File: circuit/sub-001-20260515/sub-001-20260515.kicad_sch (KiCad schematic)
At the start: 51 parts, among them SW1 SW_SPDT, SW2 SW_SPDT, SW3 SW_SPDT, U10 LD1117S12TR_SOT223, U11 LD1117S12TR_SOT223, U12 LD1117S12TR_SOT223, U13 TSSP58038, U14 TSSP58038, U15 TSSP58038, U16 TSSP58038, U8 LD1117S12TR_SOT223, U9 LD1117S12TR_SOT223

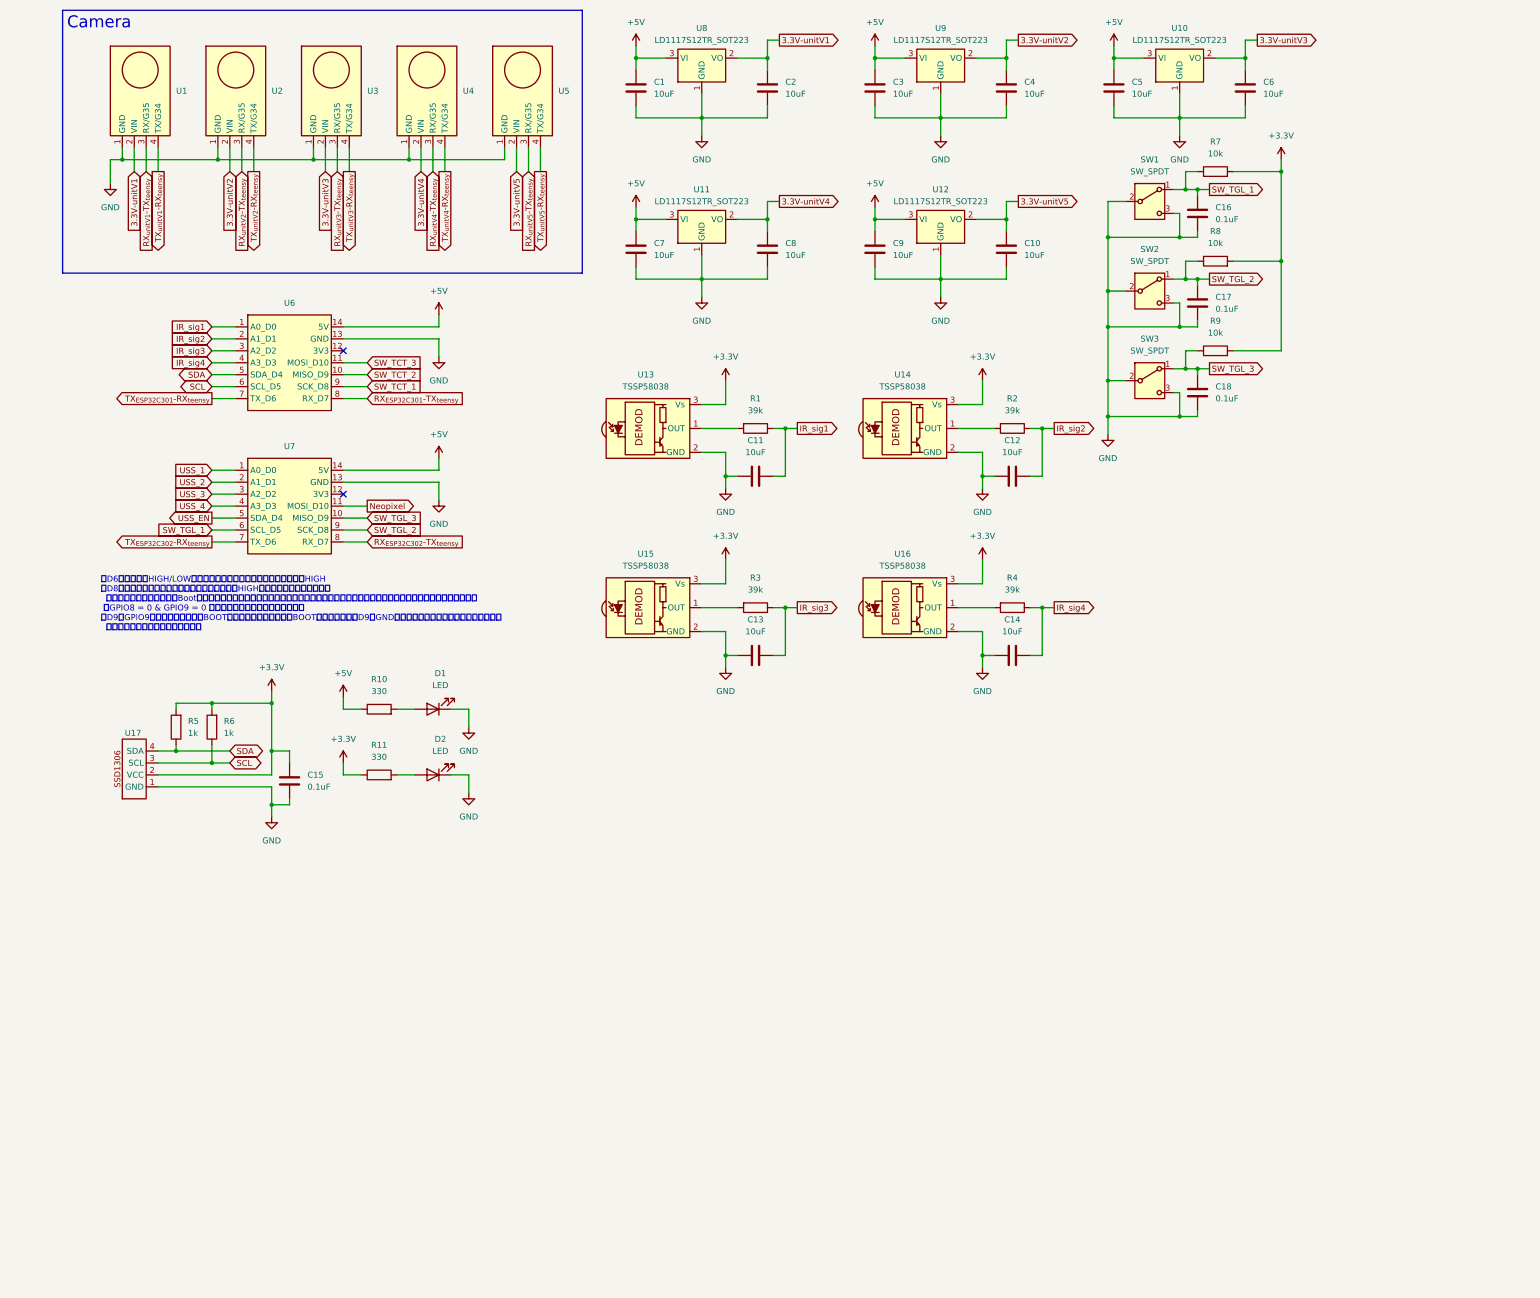
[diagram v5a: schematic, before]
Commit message: Update サブ基板の回路図を修正した、コネクタを追加できていないので後でやる
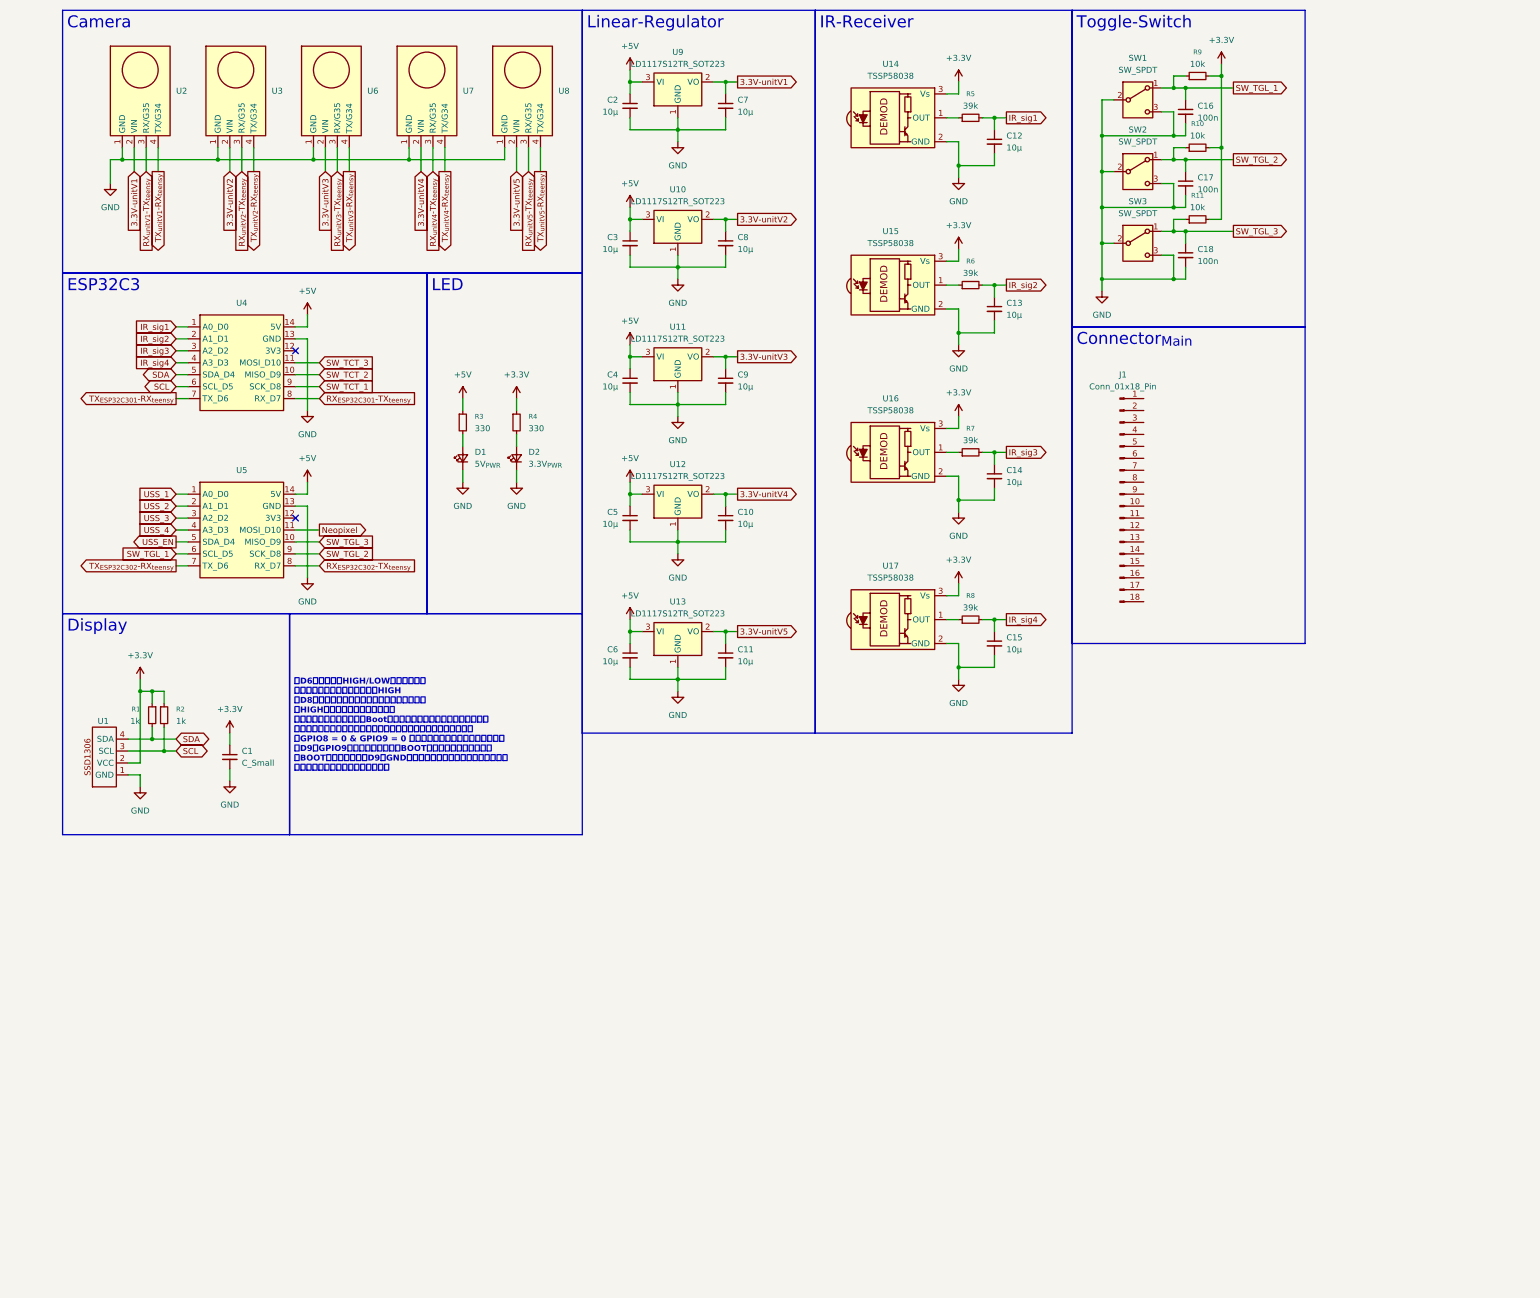
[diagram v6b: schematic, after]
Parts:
- removed C1, C10, C11, C12, C13, C14, C2, C3, C4, C5, C6, C7, C8, C9: 10uF, symbol Device:C
- removed C15, C16, C17, C18: 0.1uF, symbol Device:C
- removed D1, D2: LED, symbol Device:LED
- removed R1, R2, R3, R4: 39k, symbol Device:R
- removed R10, R11: 330, symbol Device:R
- removed R5, R6: 1k, symbol Device:R
- removed R7, R8, R9: 10k, symbol Device:R
- removed U14: TSSP58038, OptoDevice:Vishay_MINICAST-3Pin, symbol Sensor_Proximity:TSSP58038
- removed U9: LD1117S12TR_SOT223, Package_TO_SOT_SMD:SOT-223-3_TabPin2, symbol Regulator_Linear:LD1117S12TR_SOT223
- added C1: C_Small, symbol Device:C_Small
- added C10, C11, C12, C13, C14, C15, C2, C3, C4, C5, C6, C7, C8, C9: 10μ, symbol Device:C_Small
- added C16, C17, C18: 100n, symbol Device:C_Small
- added D1: 5V_{PWR}, symbol Device:LED_Small
- added D2: 3.3V_{PWR}, symbol Device:LED_Small
- added J1: Conn_01x18_Pin, symbol Connector:Conn_01x18_Pin
- added R1, R2: 1k, symbol Device:R_Small
- added R10, R11, R9: 10k, symbol Device:R_Small
- added R3, R4: 330, symbol Device:R_Small
- added R5, R6, R7, R8: 39k, symbol Device:R_Small
- added U13: LD1117S12TR_SOT223, Package_TO_SOT_SMD:SOT-223-3_TabPin2, symbol Regulator_Linear:LD1117S12TR_SOT223
- added U17: TSSP58038, OptoDevice:Vishay_MINICAST-3Pin, symbol Sensor_Proximity:TSSP58038
- renumbered U17 to U1, U13 to U14, U1 to U2, U2 to U3, U6 to U4, U7 to U5, U3 to U6, U4 to U7, U5 to U8, U8 to U9
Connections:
- net +3.3V: now also C1.1, R1.1, R10.2, R11.2, R2.1, R4.1, R9.2, U17.3 (Vs)
- net +5V: now also C2.1, C3.1, C4.1, C5.1, C6.1, R3.1, U13.3 (VI)
- net 3.3V-unitV1: now also C7.1
- net 3.3V-unitV2: now also U10.2 (VO), C8.1
- net 3.3V-unitV3: now also U11.2 (VO), C9.1; no longer U10.2 (VO)
- net 3.3V-unitV4: now also U12.2 (VO), C10.1; no longer U11.2 (VO)
- net 3.3V-unitV5: now also C11.1, U13.2 (VO); no longer U12.2 (VO)
- net GND: now also C1.2, C10.2, C11.2, C12.2, C13.2, C14.2, C15.2, C16.2, C17.2, C18.2, C2.2, C3.2, C4.2, C5.2, C6.2, C7.2, C8.2, C9.2, D1.1 (K), D2.1 (K), U13.1 (GND), U17.2 (GND)
- net IR_sig1: now also C12.1, R5.2
- net IR_sig2: now also C13.1, R6.2
- net IR_sig3: now also C14.1, R7.2
- net IR_sig4: now also C15.1, R8.2
- net SCL: now also R2.2
- net SDA: now also R1.2
- net SW_TGL_1: now also C16.1, R9.1
- net SW_TGL_2: now also C17.1, R10.1
- net SW_TGL_3: now also C18.1, R11.1
- net at U16.1 (OUT): now also R7.1
- net at U14.1 (OUT): now also R5.1
- net at U15.1 (OUT): now also R6.1
- new net: D2.2 (A), R4.2
- new net: R8.1, U17.1 (OUT)
- new net: D1.2 (A), R3.2
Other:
- note removed: "・D6は起動時にHIGH/LOWしてしまい、通信していない待機時は常にHIGH ・D8はプログラムの書き込みモードにした際に、HIGHになっている必要がある。 書き込みモードへの移行（Bootボタンを押しながらリセットする）を行う場合は、プルアップ抵抗をつけておくのがベターだそうです。 （GPIO8 = 0 & GPIO9 = 0 になると予期せぬ動きをする模様） ・D9はGPIO9とプルアップ抵抗、BOOTボタンに繋がっており、BOOTボタンを押すとD9がGNDに接続してしまうため、用途は限定的。 スイッチ入力に使うのがおすすめ。"
- moved on the sheet: SW1, U1, U14, U4, U5, U9

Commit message: Update サブ基板更新
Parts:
- removed J1: Conn_01x18_Pin, symbol Connector:Conn_01x18_Pin
- added J1: Conn_Main, symbol Connector:Conn_01x18_Socket
- added J2: Conn_NeoPixel, symbol Connector:Conn_01x12_Socket
- added J3: Conn_SW_TGL, symbol Connector:Conn_01x03_Socket
- added J4: Conn_Power, symbol Connector:Conn_01x02_Socket
- C1: value C_Small -> 100n
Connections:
- net +3.3V: now also J1.10 (Pin_10), J2.3 (Pin_3)
- net +5V: now also J1.11 (Pin_11), J2.1 (Pin_1), J2.2 (Pin_2), J4.1 (Pin_1)
- net GND: now also J1.12 (Pin_12), J2.4 (Pin_4), J2.5 (Pin_5), J4.2 (Pin_2)
- net SCL: now also J2.7 (Pin_7)
- net SDA: now also J2.6 (Pin_6)
- net SW_TGL_1: now also J3.1 (Pin_1)
- net SW_TGL_2: now also J3.2 (Pin_2)
- net SW_TGL_3: now also J3.3 (Pin_3)
- net Neopixel renamed SIG_{NeoPixel}
- net SIG_{NeoPixel}: now also J2.12 (Pin_12)
- net RX_{unitV1}-TX_{teensy}: no longer names the net of U2.3 (RX/G35)
- net RX_{unitV2}-TX_{teensy}: no longer names the net of U3.3 (RX/G35)
- net RX_{unitV3}-TX_{teensy} renamed TX_{teensy}-RX_{unitV3}
- net TX_{teensy}-RX_{unitV3}: now also J1.16 (Pin_16)
- net RX_{unitV4}-TX_{teensy} renamed TX_{teensy}-RX_{unitV4}
- net TX_{teensy}-RX_{unitV4}: now also J1.17 (Pin_17)
- net RX_{unitV5}-TX_{teensy}: no longer names the net of U8.3 (RX/G35)
- net TX_{unitV1}-RX_{teensy}: no longer names the net of U2.4 (TX/G34)
- net TX_{unitV2}-RX_{teensy}: no longer names the net of U3.4 (TX/G34)
- net TX_{unitV3}-RX_{teensy} renamed RX_{teensy}-TX_{unitV3}
- net RX_{teensy}-TX_{unitV3}: now also J1.15 (Pin_15)
- net TX_{unitV4}-RX_{teensy} renamed RX_{teensy}-TX_{unitV4}
- net RX_{teensy}-TX_{unitV4}: now also J1.18 (Pin_18)
- net TX_{unitV5}-RX_{teensy}: no longer names the net of U8.4 (TX/G34)
- new net RX_{teensy}-TX_{ESP32C301}: J1.13 (Pin_13)
- new net RX_{teensy}-TX_{ESP32C302}: J1.5 (Pin_5)
- new net RX_{teensy}-TX_{unitV1}: J1.4 (Pin_4)
- new net RX_{teensy}-TX_{unitV2}: J1.2 (Pin_2)
- new net RX_{teensy}-TX_{unitV5}: J1.9 (Pin_9)
- new net SW_{START}: J1.8 (Pin_8)
- new net SW_{TCT1}: J2.8 (Pin_8)
- new net SW_{TCT2}: J2.9 (Pin_9)
- new net SW_{TCT3}: J2.10 (Pin_10)
- new net SW_{TCT4}: J2.11 (Pin_11)
- new net TX_{teensy}-RX_{ESP32C301}: J1.14 (Pin_14)
- new net TX_{teensy}-RX_{ESP32C302}: J1.6 (Pin_6)
- new net TX_{teensy}-RX_{unitV1}: J1.3 (Pin_3)
- new net TX_{teensy}-RX_{unitV2}: J1.1 (Pin_1)
- new net TX_{teensy}-RX_{unitV5}: J1.7 (Pin_7)
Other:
- note added: "Move This To the Power-Board!!!!!"
- moved on the sheet: C16, C17, C18, R10, R11, R9, SW1, SW2, SW3

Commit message: Update サブ基板をちょっと編集
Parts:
- C1, C10, C11, C12, C13, C14, C15, C16, C17, C18, C2, C3, C4, C5, C6, C7, C8, C9: footprint (none) -> Capacitor_SMD:C_0805_2012Metric
- D1, D2: footprint (none) -> LED_SMD:LED_0603_1608Metric
- J4: footprint (none) -> Connector_AMASS:AMASS_XT30U-M_1x02_P5.0mm_Vertical
- R1, R10, R11, R2, R3, R4, R5, R6, R7, R8, R9: footprint (none) -> Resistor_SMD:R_0805_2012Metric
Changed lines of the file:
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@@
 			)
 		)
-		(property "Footprint" ""
+		(property "Footprint" "Capacitor_SMD:C_0805_2012Metric"
 			(at 153.67 33.02 0)
 			(hide yes)
@@
 			)
 		)
-		(property "Footprint" ""
+		(property "Footprint" "Resistor_SMD:R_0805_2012Metric"
 			(at 109.22 100.33 0)
 			(hide yes)
@@
 			)
 		)
-		(property "Footprint" ""
+		(property "Footprint" "Resistor_SMD:R_0805_2012Metric"
 			(at 205.74 71.12 0)
 			(hide yes)
@@
 			)
 		)
-		(property "Footprint" ""
+		(property "Footprint" "Capacitor_SMD:C_0805_2012Metric"
 			(at 133.35 120.65 0)
 			(hide yes)
@@
 			)
 		)
-		(property "Footprint" ""
+		(property "Footprint" "Resistor_SMD:R_0805_2012Metric"
 			(at 205.74 35.56 0)
 			(hide yes)
@@
 			)
 		)
-		(property "Footprint" ""
+		(property "Footprint" "Capacitor_SMD:C_0805_2012Metric"
 			(at 133.35 91.44 0)
 			(hide yes)
@@
 			)
 		)
-		(property "Footprint" ""
+		(property "Footprint" "Capacitor_SMD:C_0805_2012Metric"
 			(at 250.19 254 0)
 			(hide yes)
@@
 			)
 		)
-		(property "Footprint" ""
+		(property "Footprint" "Capacitor_SMD:C_0805_2012Metric"
 			(at 153.67 62.23 0)
 			(hide yes)
@@
 			)
 		)
-		(property "Footprint" ""
+		(property "Footprint" "Capacitor_SMD:C_0805_2012Metric"
 			(at 210.82 111.76 0)
 			(hide yes)
@@
 			)
 		)
-		(property "Footprint" ""
+		(property "Footprint" "Connector_AMASS:AMASS_XT30U-M_1x02_P5.0mm_Vertical"
 			(at 290.83 29.21 0)
 			(hide yes)
@@
 			)
 		)
-		(property "Footprint" ""
+		(property "Footprint" "Capacitor_SMD:C_0805_2012Metric"
 			(at 133.35 33.02 0)
 			(hide yes)
@@
 			)
 		)
-		(property "Footprint" ""
+		(property "Footprint" "Capacitor_SMD:C_0805_2012Metric"
 			(at 133.35 62.23 0)
 			(hide yes)
@@
 			)
 		)
-		(property "Footprint" ""
+		(property "Footprint" "Capacitor_SMD:C_0805_2012Metric"
 			(at 210.82 76.2 0)
 			(hide yes)
@@
 			)
 		)
-		(property "Footprint" ""
+		(property "Footprint" "Resistor_SMD:R_0805_2012Metric"
 			(at 205.74 106.68 0)
 			(hide yes)
@@
 			)
 		)
-		(property "Footprint" ""
+		(property "Footprint" "Capacitor_SMD:C_0805_2012Metric"
 			(at 153.67 149.86 0)
 			(hide yes)
@@
 			)
 		)
-		(property "Footprint" ""
+		(property "Footprint" "Capacitor_SMD:C_0805_2012Metric"
 			(at 250.19 269.24 0)
 			(hide yes)
@@
 			)
 		)
-		(property "Footprint" ""
+		(property "Footprint" "LED_SMD:LED_0603_1608Metric"
 			(at 109.22 107.95 90)
 			(hide yes)
@@
 			)
 		)
-		(property "Footprint" ""
+		(property "Footprint" "Capacitor_SMD:C_0805_2012Metric"
 			(at 210.82 40.64 0)
 			(hide yes)
@@
 			)
 		)
-		(property "Footprint" ""
+		(property "Footprint" "Resistor_SMD:R_0805_2012Metric"
 			(at 31.75 162.56 0)
 			(hide yes)
@@
 			)
 		)
-		(property "Footprint" ""
+		(property "Footprint" "Resistor_SMD:R_0805_2012Metric"
 			(at 252.73 231.14 0)
 			(hide yes)
@@
 			)
 		)
-		(property "Footprint" ""
+		(property "Footprint" "Capacitor_SMD:C_0805_2012Metric"
 			(at 48.26 171.45 0)
 			(hide yes)
@@
 			)
 		)
-		(property "Footprint" ""
+		(property "Footprint" "Capacitor_SMD:C_0805_2012Metric"
 			(at 133.35 149.86 0)
 			(hide yes)
@@
 			)
 		)
-		(property "Footprint" ""
+		(property "Footprint" "Resistor_SMD:R_0805_2012Metric"
 			(at 34.29 162.56 0)
 			(hide yes)
@@
 			)
 		)
-		(property "Footprint" ""
+		(property "Footprint" "LED_SMD:LED_0603_1608Metric"
 			(at 97.79 107.95 90)
 			(hide yes)
@@
 			)
 		)
-		(property "Footprint" ""
+		(property "Footprint" "Resistor_SMD:R_0805_2012Metric"
 			(at 252.73 246.38 0)
 			(hide yes)
@@
 			)
 		)
-		(property "Footprint" ""
+		(property "Footprint" "Resistor_SMD:R_0805_2012Metric"
 			(at 205.74 142.24 0)
 			(hide yes)
@@
 			)
 		)
-		(property "Footprint" ""
+		(property "Footprint" "Capacitor_SMD:C_0805_2012Metric"
 			(at 153.67 91.44 0)
 			(hide yes)
@@
 			)
 		)
-		(property "Footprint" ""
+		(property "Footprint" "Capacitor_SMD:C_0805_2012Metric"
 			(at 153.67 120.65 0)
 			(hide yes)
@@
 			)
 		)
-		(property "Footprint" ""
+		(property "Footprint" "Resistor_SMD:R_0805_2012Metric"
 			(at 252.73 261.62 0)
 			(hide yes)
@@
 			)
 		)
-		(property "Footprint" ""
+		(property "Footprint" "Capacitor_SMD:C_0805_2012Metric"
 			(at 210.82 147.32 0)
 			(hide yes)
@@
 			)
 		)
-		(property "Footprint" ""
+		(property "Footprint" "Capacitor_SMD:C_0805_2012Metric"
 			(at 250.19 238.76 0)
 			(hide yes)
@@
 			)
 		)
-		(property "Footprint" ""
+		(property "Footprint" "Resistor_SMD:R_0805_2012Metric"
 			(at 97.79 100.33 0)
 			(hide yes)
